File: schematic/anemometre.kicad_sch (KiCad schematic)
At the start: 38 parts, among them J1 Anemometre, J10 PWR_SEL, J2 AVR-ISP-6, J3 PORT_C_ADC, J4 PORT_B, J5 Opto_PB0, J6 TTL Serial, J7 INTs/Ts, J8 USB_B_Mini, J9 +5VDC, SW1 Reset, U1 ATmega328P-P, U2 4N25, U3 FT232RL, Y1 8MHz

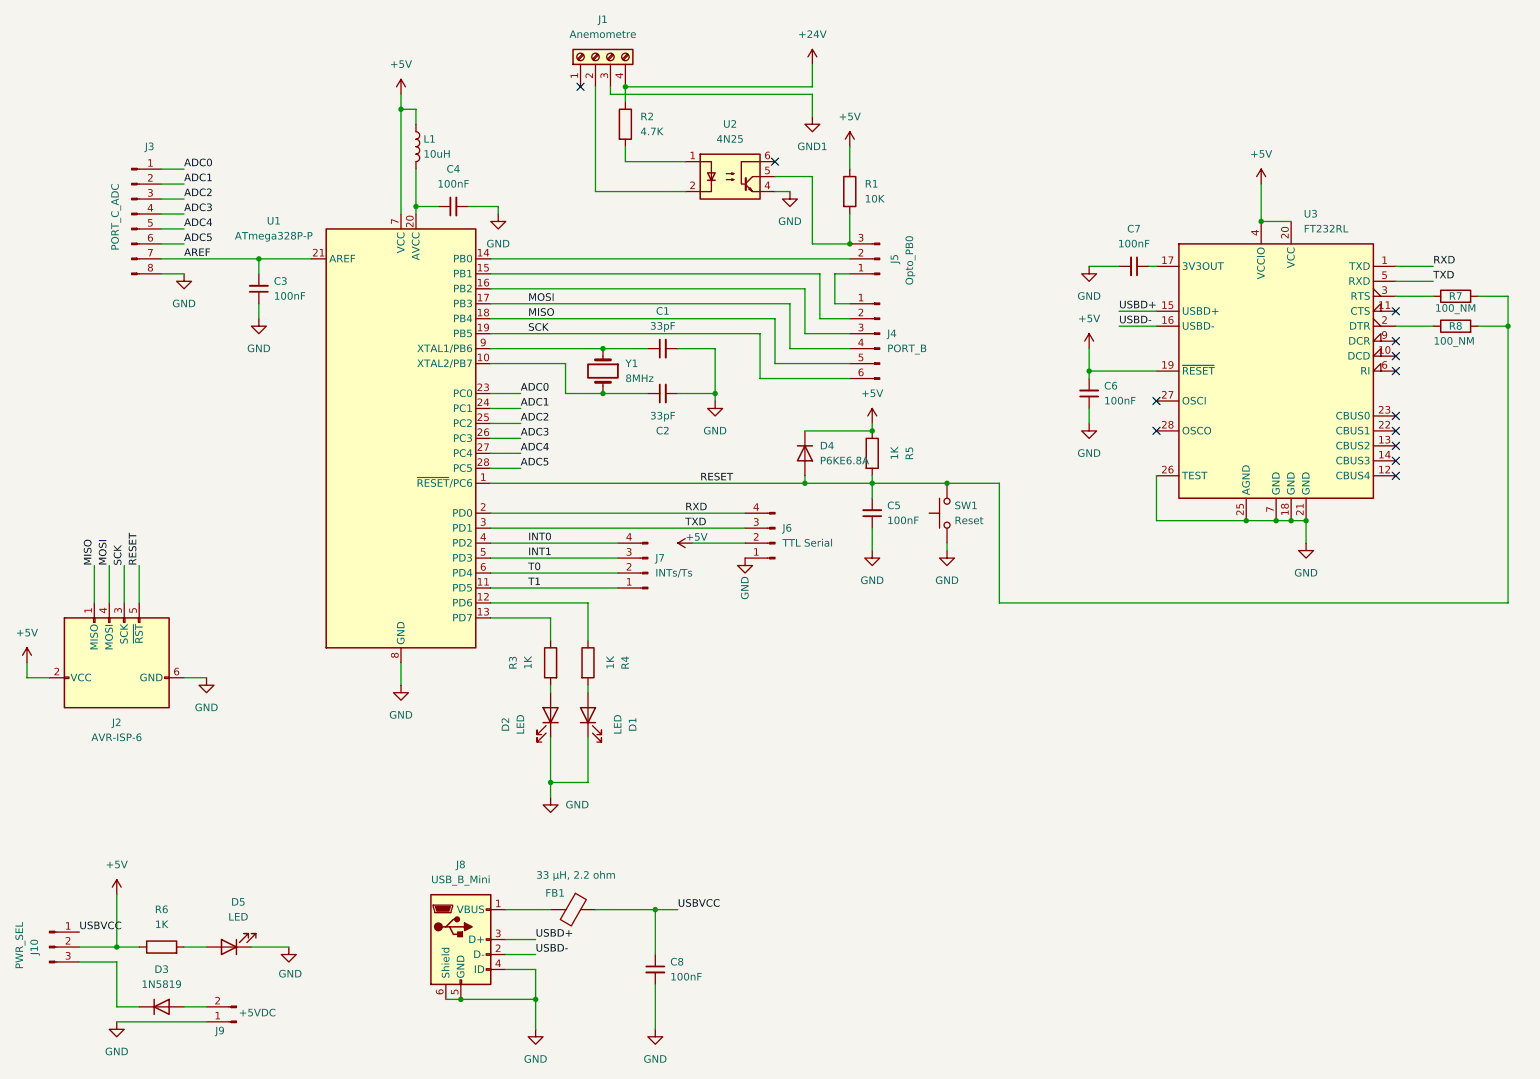
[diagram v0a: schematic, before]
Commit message: Schematic and PCB upgraded to support temperature and rain sensors
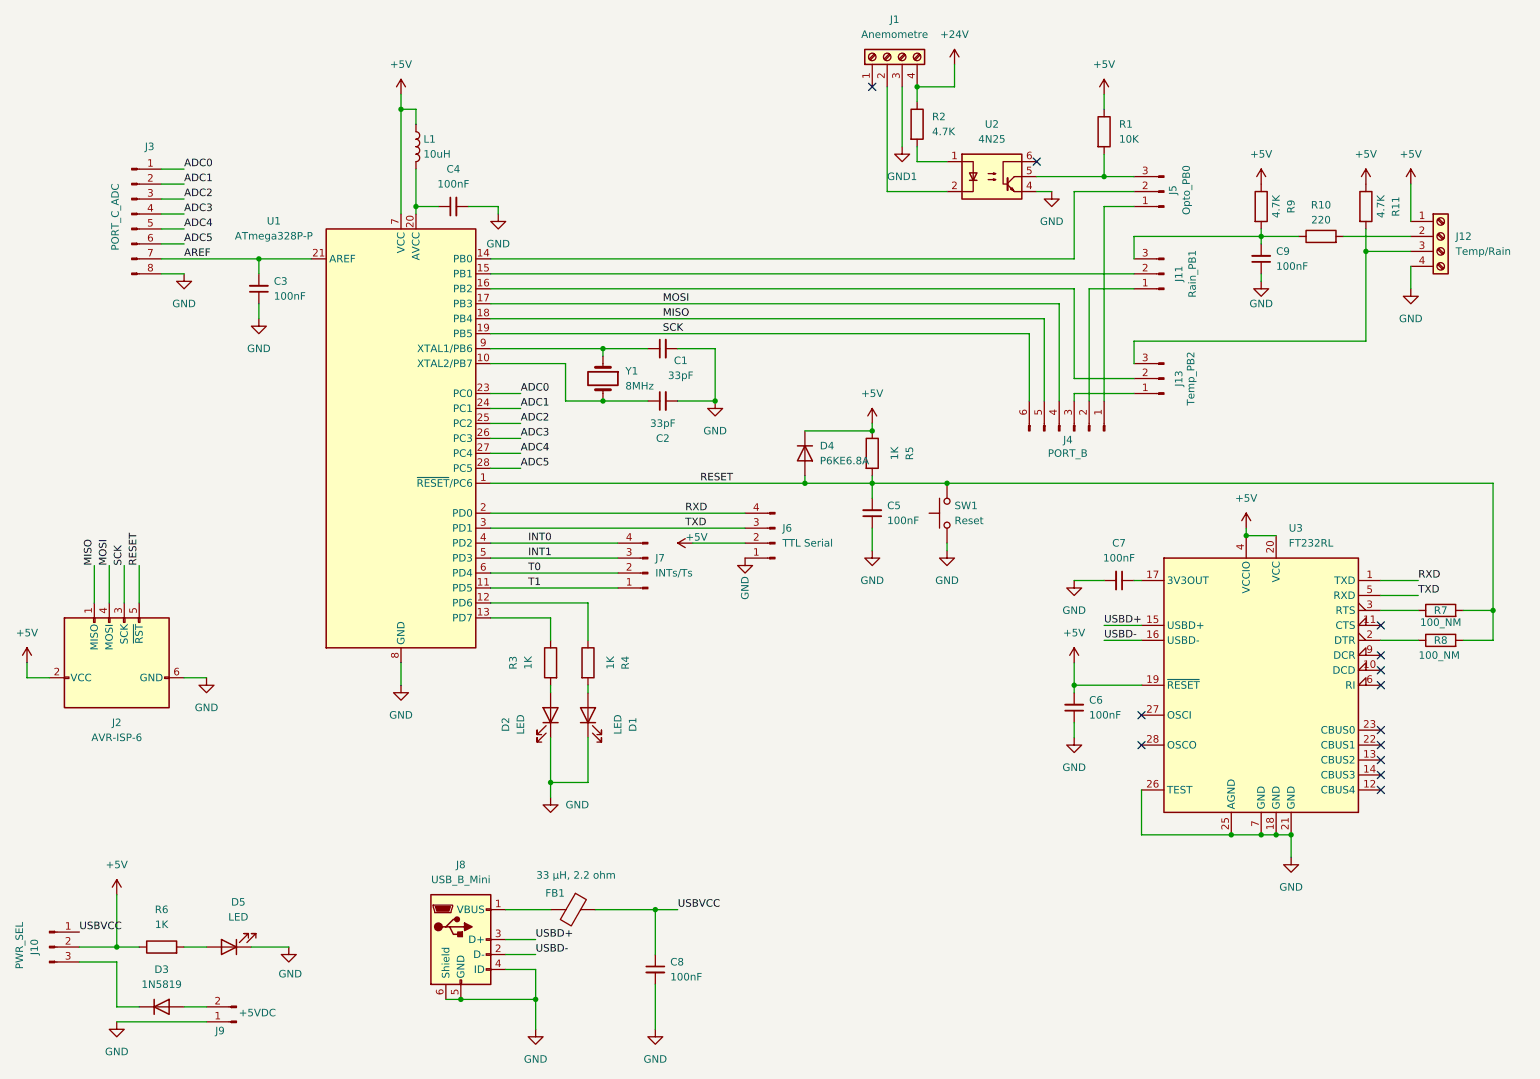
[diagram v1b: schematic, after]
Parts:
- added C9: 100nF, Capacitor_THT:C_Disc_D7.0mm_W2.5mm_P5.00mm, symbol Device:C_Small
- added J11: Rain_PB1, Connector_PinHeader_2.54mm:PinHeader_1x03_P2.54mm_Vertical, symbol Connector:Conn_01x03_Pin
- added J12: Temp/Rain, TerminalBlock_Phoenix:TerminalBlock_Phoenix_MKDS-1,5-4-5.08_1x04_P5.08mm_Horizontal, symbol Connector:Screw_Terminal_01x04
- added J13: Temp_PB2, Connector_PinHeader_2.54mm:PinHeader_1x03_P2.54mm_Vertical, symbol Connector:Conn_01x03_Pin
- added R10: 220, Resistor_THT:R_Axial_DIN0204_L3.6mm_D1.6mm_P7.62mm_Horizontal, symbol Device:R
- added R11, R9: 4.7K, Resistor_THT:R_Axial_DIN0204_L3.6mm_D1.6mm_P7.62mm_Horizontal, symbol Device:R
- D1: Color (none) -> Green
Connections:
- net +5V: now also J12.1 (Pin_1), R11.1, R9.1
- net GND: now also C9.1, J12.4 (Pin_4)
- net at J4.2 (Pin_2): now also J11.1 (Pin_1); no longer U1.15 (PB1)
- net at J4.3 (Pin_3): now also J13.1 (Pin_1); no longer U1.16 (PB2)
- new net: C9.2, J11.3 (Pin_3), R10.1, R9.2
- new net: J12.2 (Pin_2), R10.2
- new net: J12.3 (Pin_3), J13.3 (Pin_3), R11.2
- new net: J13.2 (Pin_2), U1.16 (PB2)
- new net: J11.2 (Pin_2), U1.15 (PB1)
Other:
- moved on the sheet: C2, C6, C7, J1, J4, J5, R1, R2, R7, R8, U2, U3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
